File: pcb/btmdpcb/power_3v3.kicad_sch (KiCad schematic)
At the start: 6 parts, among them U2 ME6211C33M5

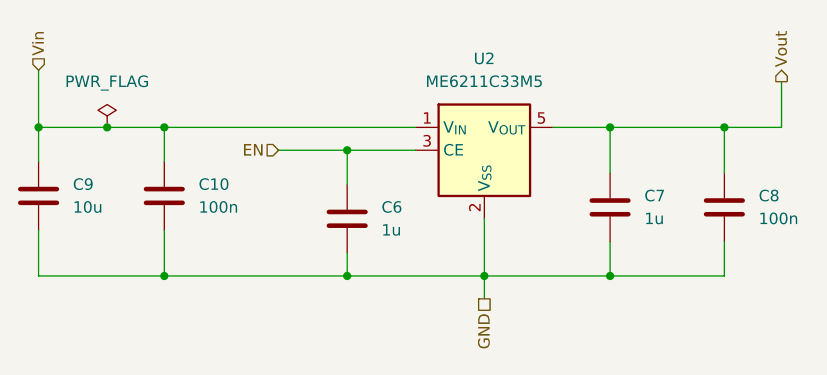
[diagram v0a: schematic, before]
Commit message: Clean up schematic, implement all logic functionality
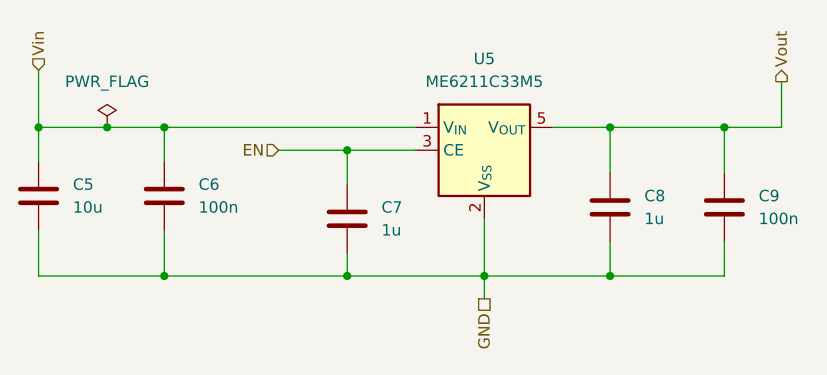
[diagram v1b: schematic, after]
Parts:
- renumbered C9 to C5, C10 to C6, C6 to C7, C7 to C8, C8 to C9, U2 to U5
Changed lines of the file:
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@@
 		(dnp no)
 		(fields_autoplaced yes)
-		(property "Reference" "#FLG04"
+		(property "Reference" "#FLG07"
 			(at 99.06 83.185 0)
 			(effects
@@
 			(project ""
 				(path "/6e43e92f-e106-411c-86ee-217d084aee5b/607b6f64-44e5-4f00-b0ca-53e53733045d"
-					(reference "#FLG04")
+					(reference "#FLG07")
 					(unit 1)
 				)
@@
 		(dnp no)
 		(fields_autoplaced yes)
-		(property "Reference" "C10"
+		(property "Reference" "C6"
 			(at 109.22 91.4399 0)
 			(effects
@@
 			(project "btmdpcb"
 				(path "/6e43e92f-e106-411c-86ee-217d084aee5b/607b6f64-44e5-4f00-b0ca-53e53733045d"
-					(reference "C10")
+					(reference "C6")
 					(unit 1)
 				)
@@
 		(dnp no)
 		(fields_autoplaced yes)
-		(property "Reference" "U2"
+		(property "Reference" "U5"
 			(at 140.97 77.47 0)
 			(effects
@@
 			(project "btmdpcb"
 				(path "/6e43e92f-e106-411c-86ee-217d084aee5b/607b6f64-44e5-4f00-b0ca-53e53733045d"
-					(reference "U2")
+					(reference "U5")
 					(unit 1)
 				)
@@
 		(dnp no)
 		(fields_autoplaced yes)
-		(property "Reference" "C9"
+		(property "Reference" "C5"
 			(at 95.25 91.4399 0)
 			(effects
@@
 			(project "btmdpcb"
 				(path "/6e43e92f-e106-411c-86ee-217d084aee5b/607b6f64-44e5-4f00-b0ca-53e53733045d"
-					(reference "C9")
+					(reference "C5")
 					(unit 1)
 				)
@@
 		(dnp no)
 		(fields_autoplaced yes)
-		(property "Reference" "C8"
+		(property "Reference" "C9"
 			(at 171.45 92.7099 0)
 			(effects
@@
 			(project "btmdpcb"
 				(path "/6e43e92f-e106-411c-86ee-217d084aee5b/607b6f64-44e5-4f00-b0ca-53e53733045d"
-					(reference "C8")
+					(reference "C9")
 					(unit 1)
 				)
@@
 		(dnp no)
 		(fields_autoplaced yes)
-		(property "Reference" "C6"
+		(property "Reference" "C7"
 			(at 129.54 93.9799 0)
 			(effects
@@
 			(project ""
 				(path "/6e43e92f-e106-411c-86ee-217d084aee5b/607b6f64-44e5-4f00-b0ca-53e53733045d"
-					(reference "C6")
+					(reference "C7")
 					(unit 1)
 				)
@@
 		(dnp no)
 		(fields_autoplaced yes)
-		(property "Reference" "C7"
+		(property "Reference" "C8"
 			(at 158.75 92.7099 0)
 			(effects
@@
 			(project "btmdpcb"
 				(path "/6e43e92f-e106-411c-86ee-217d084aee5b/607b6f64-44e5-4f00-b0ca-53e53733045d"
-					(reference "C7")
-					(unit 1)
-				)
+					(reference "C8")
+					(unit 1)
+				)

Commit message: Remove redundant regulators, simplify schematic
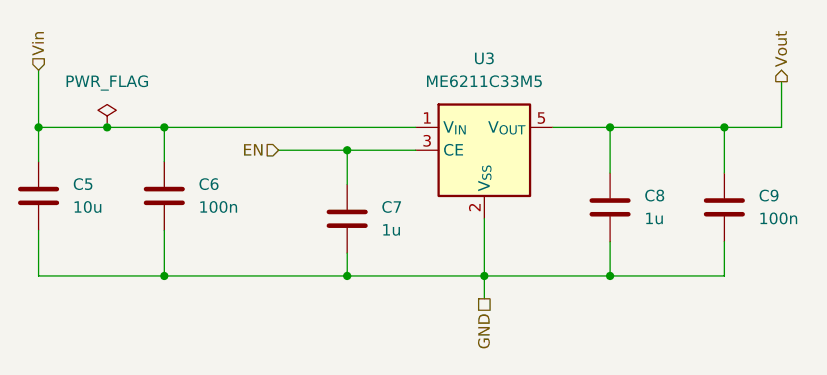
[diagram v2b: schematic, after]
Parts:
- renumbered U5 to U3
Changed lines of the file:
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@@
 		(dnp no)
 		(fields_autoplaced yes)
-		(property "Reference" "#FLG07"
+		(property "Reference" "#FLG05"
 			(at 99.06 83.185 0)
 			(effects
@@
 			(project ""
 				(path "/6e43e92f-e106-411c-86ee-217d084aee5b/607b6f64-44e5-4f00-b0ca-53e53733045d"
-					(reference "#FLG07")
+					(reference "#FLG05")
 					(unit 1)
 				)
@@
 		(dnp no)
 		(fields_autoplaced yes)
-		(property "Reference" "U5"
+		(property "Reference" "U3"
 			(at 140.97 77.47 0)
 			(effects
@@
 			(project "btmdpcb"
 				(path "/6e43e92f-e106-411c-86ee-217d084aee5b/607b6f64-44e5-4f00-b0ca-53e53733045d"
-					(reference "U5")
+					(reference "U3")
 					(unit 1)
 				)

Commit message: Add missing libraries, assign all footprints
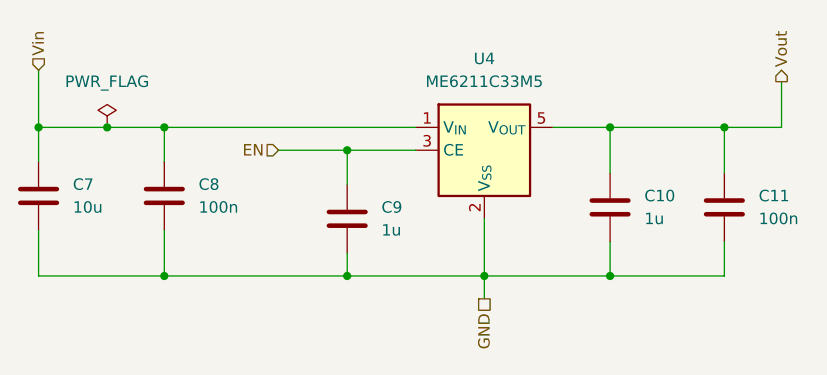
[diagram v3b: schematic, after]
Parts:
- C10: renamed from C8; footprint (none) -> Capacitor_SMD:C_0805_2012Metric_Pad1.18x1.45mm_HandSolder
- C11: renamed from C9; footprint (none) -> Capacitor_SMD:C_0805_2012Metric_Pad1.18x1.45mm_HandSolder
- C7: renamed from C5; footprint (none) -> Capacitor_SMD:C_0805_2012Metric_Pad1.18x1.45mm_HandSolder
- C8: renamed from C6; footprint (none) -> Capacitor_SMD:C_0805_2012Metric_Pad1.18x1.45mm_HandSolder
- C9: renamed from C7; footprint (none) -> Capacitor_SMD:C_0805_2012Metric_Pad1.18x1.45mm_HandSolder
- renumbered U3 to U4
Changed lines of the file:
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@@
 		(dnp no)
 		(fields_autoplaced yes)
-		(property "Reference" "C6"
+		(property "Reference" "C8"
 			(at 109.22 91.4399 0)
 			(effects
@@
 			)
 		)
-		(property "Footprint" ""
+		(property "Footprint" "Capacitor_SMD:C_0805_2012Metric_Pad1.18x1.45mm_HandSolder"
 			(at 106.3752 96.52 0)
 			(effects
@@
 			(project "btmdpcb"
 				(path "/6e43e92f-e106-411c-86ee-217d084aee5b/607b6f64-44e5-4f00-b0ca-53e53733045d"
-					(reference "C6")
+					(reference "C8")
 					(unit 1)
 				)
@@
 		(dnp no)
 		(fields_autoplaced yes)
-		(property "Reference" "U3"
+		(property "Reference" "U4"
 			(at 140.97 77.47 0)
 			(effects
@@
 			(project "btmdpcb"
 				(path "/6e43e92f-e106-411c-86ee-217d084aee5b/607b6f64-44e5-4f00-b0ca-53e53733045d"
-					(reference "U3")
+					(reference "U4")
 					(unit 1)
 				)
@@
 		(dnp no)
 		(fields_autoplaced yes)
-		(property "Reference" "C5"
+		(property "Reference" "C7"
 			(at 95.25 91.4399 0)
 			(effects
@@
 			)
 		)
-		(property "Footprint" ""
+		(property "Footprint" "Capacitor_SMD:C_0805_2012Metric_Pad1.18x1.45mm_HandSolder"
 			(at 92.4052 96.52 0)
 			(effects
@@
 			(project "btmdpcb"
 				(path "/6e43e92f-e106-411c-86ee-217d084aee5b/607b6f64-44e5-4f00-b0ca-53e53733045d"
-					(reference "C5")
+					(reference "C7")
 					(unit 1)
 				)
@@
 		(dnp no)
 		(fields_autoplaced yes)
-		(property "Reference" "C9"
+		(property "Reference" "C11"
 			(at 171.45 92.7099 0)
 			(effects
@@
 			)
 		)
-		(property "Footprint" ""
+		(property "Footprint" "Capacitor_SMD:C_0805_2012Metric_Pad1.18x1.45mm_HandSolder"
 			(at 168.6052 97.79 0)
 			(effects
@@
 			(project "btmdpcb"
 				(path "/6e43e92f-e106-411c-86ee-217d084aee5b/607b6f64-44e5-4f00-b0ca-53e53733045d"
-					(reference "C9")
+					(reference "C11")
 					(unit 1)
 				)
@@
 		(dnp no)
 		(fields_autoplaced yes)
-		(property "Reference" "C7"
+		(property "Reference" "C9"
 			(at 129.54 93.9799 0)
 			(effects
@@
 			)
 		)
-		(property "Footprint" ""
+		(property "Footprint" "Capacitor_SMD:C_0805_2012Metric_Pad1.18x1.45mm_HandSolder"
 			(at 126.6952 99.06 0)
 			(effects
@@
 			(project ""
 				(path "/6e43e92f-e106-411c-86ee-217d084aee5b/607b6f64-44e5-4f00-b0ca-53e53733045d"
-					(reference "C7")
+					(reference "C9")
 					(unit 1)
 				)
@@
 		(dnp no)
 		(fields_autoplaced yes)
-		(property "Reference" "C8"
+		(property "Reference" "C10"
 			(at 158.75 92.7099 0)
 			(effects
@@
 			)
 		)
-		(property "Footprint" ""
+		(property "Footprint" "Capacitor_SMD:C_0805_2012Metric_Pad1.18x1.45mm_HandSolder"
 			(at 155.9052 97.79 0)
 			(effects
@@
 			(project "btmdpcb"
 				(path "/6e43e92f-e106-411c-86ee-217d084aee5b/607b6f64-44e5-4f00-b0ca-53e53733045d"
-					(reference "C8")
-					(unit 1)
-				)
+					(reference "C10")
+					(unit 1)
+				)

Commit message: Correct footprints, fix issues on update PCB from schematic
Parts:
- U4: footprint Package_TO_SOT_SMD:SOT-23-5 -> Package_TO_SOT_SMD:SOT-23-5_HandSoldering
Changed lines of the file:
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@@
 			)
 		)
-		(property "Footprint" "Package_TO_SOT_SMD:SOT-23-5"
+		(property "Footprint" "Package_TO_SOT_SMD:SOT-23-5_HandSoldering"
 			(at 140.462 101.092 0)
 			(effects

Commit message: Layout PCB
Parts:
- added TP10: 3V3_IN, TestPoint:TestPoint_Pad_D1.0mm, symbol Connector:TestPoint
- added TP11: 3V3_OUT, TestPoint:TestPoint_Pad_D1.0mm, symbol Connector:TestPoint
- renumbered C8 to C10, C9 to C11, C10 to C12, C11 to C13, C7 to C9
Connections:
- net Vin: now also TP10.1
- net Vout: now also TP11.1
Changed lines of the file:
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@@
+	)
+	(junction
+		(at 157.48 85.09)
+		(diameter 0)
+		(color 0 0 0 0)
 	)
 	(junction
@@
 		(color 0 0 0 0)
 	)
+	(junction
+		(at 119.38 85.09)
+		(diameter 0)
+		(color 0 0 0 0)
+	)
 	(wire
 		(pts
@@
 	(wire
 		(pts
-			(xy 154.94 85.09) (xy 167.64 85.09)
+			(xy 154.94 85.09) (xy 157.48 85.09)
 		)
 		(stroke
@@
 	(wire
 		(pts
+			(xy 119.38 83.82) (xy 119.38 85.09)
+		)
+		(stroke
+			(width 0)
+			(type default)
+		)
+	)
+	(wire
+		(pts
 			(xy 140.97 95.25) (xy 140.97 101.6)
 		)
@@
 	(wire
 		(pts
+			(xy 157.48 85.09) (xy 167.64 85.09)
+		)
+		(stroke
+			(width 0)
+			(type default)
+		)
+	)
+	(wire
+		(pts
 			(xy 154.94 101.6) (xy 167.64 101.6)
 		)
@@
 	(wire
 		(pts
-			(xy 105.41 85.09) (xy 133.35 85.09)
+			(xy 105.41 85.09) (xy 119.38 85.09)
 		)
 		(stroke
@@
 	(wire
 		(pts
+			(xy 157.48 83.82) (xy 157.48 85.09)
+		)
+		(stroke
+			(width 0)
+			(type default)
+		)
+	)
+	(wire
+		(pts
 			(xy 91.44 96.52) (xy 91.44 101.6)
 		)
@@
 		(pts
 			(xy 105.41 101.6) (xy 125.73 101.6)
+		)
+		(stroke
+			(width 0)
+			(type default)
+		)
+	)
+	(wire
+		(pts
+			(xy 119.38 85.09) (xy 133.35 85.09)
 		)
 		(stroke
@@
 			)
 			(justify left)
+		)
+	)
+	(symbol
+		(lib_id "Connector:TestPoint")
+		(at 157.48 83.82 0)
+		(unit 1)
+		(exclude_from_sim no)
+		(in_bom yes)
+		(on_board yes)
+		(dnp no)
+		(fields_autoplaced yes)
+		(property "Reference" "TP11"
+			(at 160.02 79.2479 0)
+			(effects
+				(font
+					(size 1.27 1.27)
+				)
+				(justify left)
+			)
+		)
+		(property "Value" "3V3_OUT"
+			(at 160.02 81.7879 0)
+			(effects
+				(font
+					(size 1.27 1.27)
+				)
+				(justify left)
+			)
+		)
+		(property "Footprint" "TestPoint:TestPoint_Pad_D1.0mm"
+			(at 162.56 83.82 0)
+			(effects
+				(font
+					(size 1.27 1.27)
+				)
+				(hide yes)
+			)
+		)
+		(property "Datasheet" "~"
+			(at 162.56 83.82 0)
+			(effects
+				(font
+					(size 1.27 1.27)
+				)
+				(hide yes)
+			)
+		)
+		(property "Description" "test point"
+			(at 157.48 83.82 0)
+			(effects
+				(font
+					(size 1.27 1.27)
+				)
+				(hide yes)
+			)
+		)
+		(pin "1"
+		)
+		(instances
+			(project "btmdpcb"
+				(path "/6e43e92f-e106-411c-86ee-217d084aee5b/607b6f64-44e5-4f00-b0ca-53e53733045d"
+					(reference "TP11")
+					(unit 1)
+				)
+			)
 		)
 	)
@@
 		(dnp no)
 		(fields_autoplaced yes)
-		(property "Reference" "C8"
+		(property "Reference" "C10"
 			(at 109.22 91.4399 0)
 			(effects
@@
 			(project "btmdpcb"
 				(path "/6e43e92f-e106-411c-86ee-217d084aee5b/607b6f64-44e5-4f00-b0ca-53e53733045d"
-					(reference "C8")
+					(reference "C10")
+					(unit 1)
+				)
+			)
+		)
+	)
+	(symbol
+		(lib_id "Connector:TestPoint")
+		(at 119.38 83.82 0)
+		(unit 1)
+		(exclude_from_sim no)
+		(in_bom yes)
+		(on_board yes)
+		(dnp no)
+		(fields_autoplaced yes)
+		(property "Reference" "TP10"
+			(at 121.92 79.2479 0)
+			(effects
+				(font
+					(size 1.27 1.27)
+				)
+				(justify left)
+			)
+		)
+		(property "Value" "3V3_IN"
+			(at 121.92 81.7879 0)
+			(effects
+				(font
+					(size 1.27 1.27)
+				)
+				(justify left)
+			)
+		)
+		(property "Footprint" "TestPoint:TestPoint_Pad_D1.0mm"
+			(at 124.46 83.82 0)
+			(effects
+				(font
+					(size 1.27 1.27)
+				)
+				(hide yes)
+			)
+		)
+		(property "Datasheet" "~"
+			(at 124.46 83.82 0)
+			(effects
+				(font
+					(size 1.27 1.27)
+				)
+				(hide yes)
+			)
+		)
+		(property "Description" "test point"
+			(at 119.38 83.82 0)
+			(effects
+				(font
+					(size 1.27 1.27)
+				)
+				(hide yes)
+			)
+		)
+		(pin "1"
+		)
+		(instances
+			(project "btmdpcb"
+				(path "/6e43e92f-e106-411c-86ee-217d084aee5b/607b6f64-44e5-4f00-b0ca-53e53733045d"
+					(reference "TP10")
 					(unit 1)
 				)
@@
 		(dnp no)
 		(fields_autoplaced yes)
-		(property "Reference" "C7"
+		(property "Reference" "C9"
 			(at 95.25 91.4399 0)
 			(effects
@@
 			(project "btmdpcb"
 				(path "/6e43e92f-e106-411c-86ee-217d084aee5b/607b6f64-44e5-4f00-b0ca-53e53733045d"
-					(reference "C7")
+					(reference "C9")
 					(unit 1)
 				)
@@
 		(dnp no)
 		(fields_autoplaced yes)
-		(property "Reference" "C11"
+		(property "Reference" "C13"
 			(at 171.45 92.7099 0)
 			(effects
@@
 			(project "btmdpcb"
 				(path "/6e43e92f-e106-411c-86ee-217d084aee5b/607b6f64-44e5-4f00-b0ca-53e53733045d"
-					(reference "C11")
+					(reference "C13")
 					(unit 1)
 				)
@@
 		(dnp no)
 		(fields_autoplaced yes)
-		(property "Reference" "C9"
+		(property "Reference" "C11"
 			(at 129.54 93.9799 0)
 			(effects
@@
 			(project ""
 				(path "/6e43e92f-e106-411c-86ee-217d084aee5b/607b6f64-44e5-4f00-b0ca-53e53733045d"
-					(reference "C9")
+					(reference "C11")
 					(unit 1)
 				)
@@
 		(dnp no)
 		(fields_autoplaced yes)
-		(property "Reference" "C10"
+		(property "Reference" "C12"
 			(at 158.75 92.7099 0)
 			(effects
@@
 			(project "btmdpcb"
 				(path "/6e43e92f-e106-411c-86ee-217d084aee5b/607b6f64-44e5-4f00-b0ca-53e53733045d"
-					(reference "C10")
+					(reference "C12")
 					(unit 1)
 				)
